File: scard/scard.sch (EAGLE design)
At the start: 49 parts, among them Q1 IRFD9210, X1 COAX

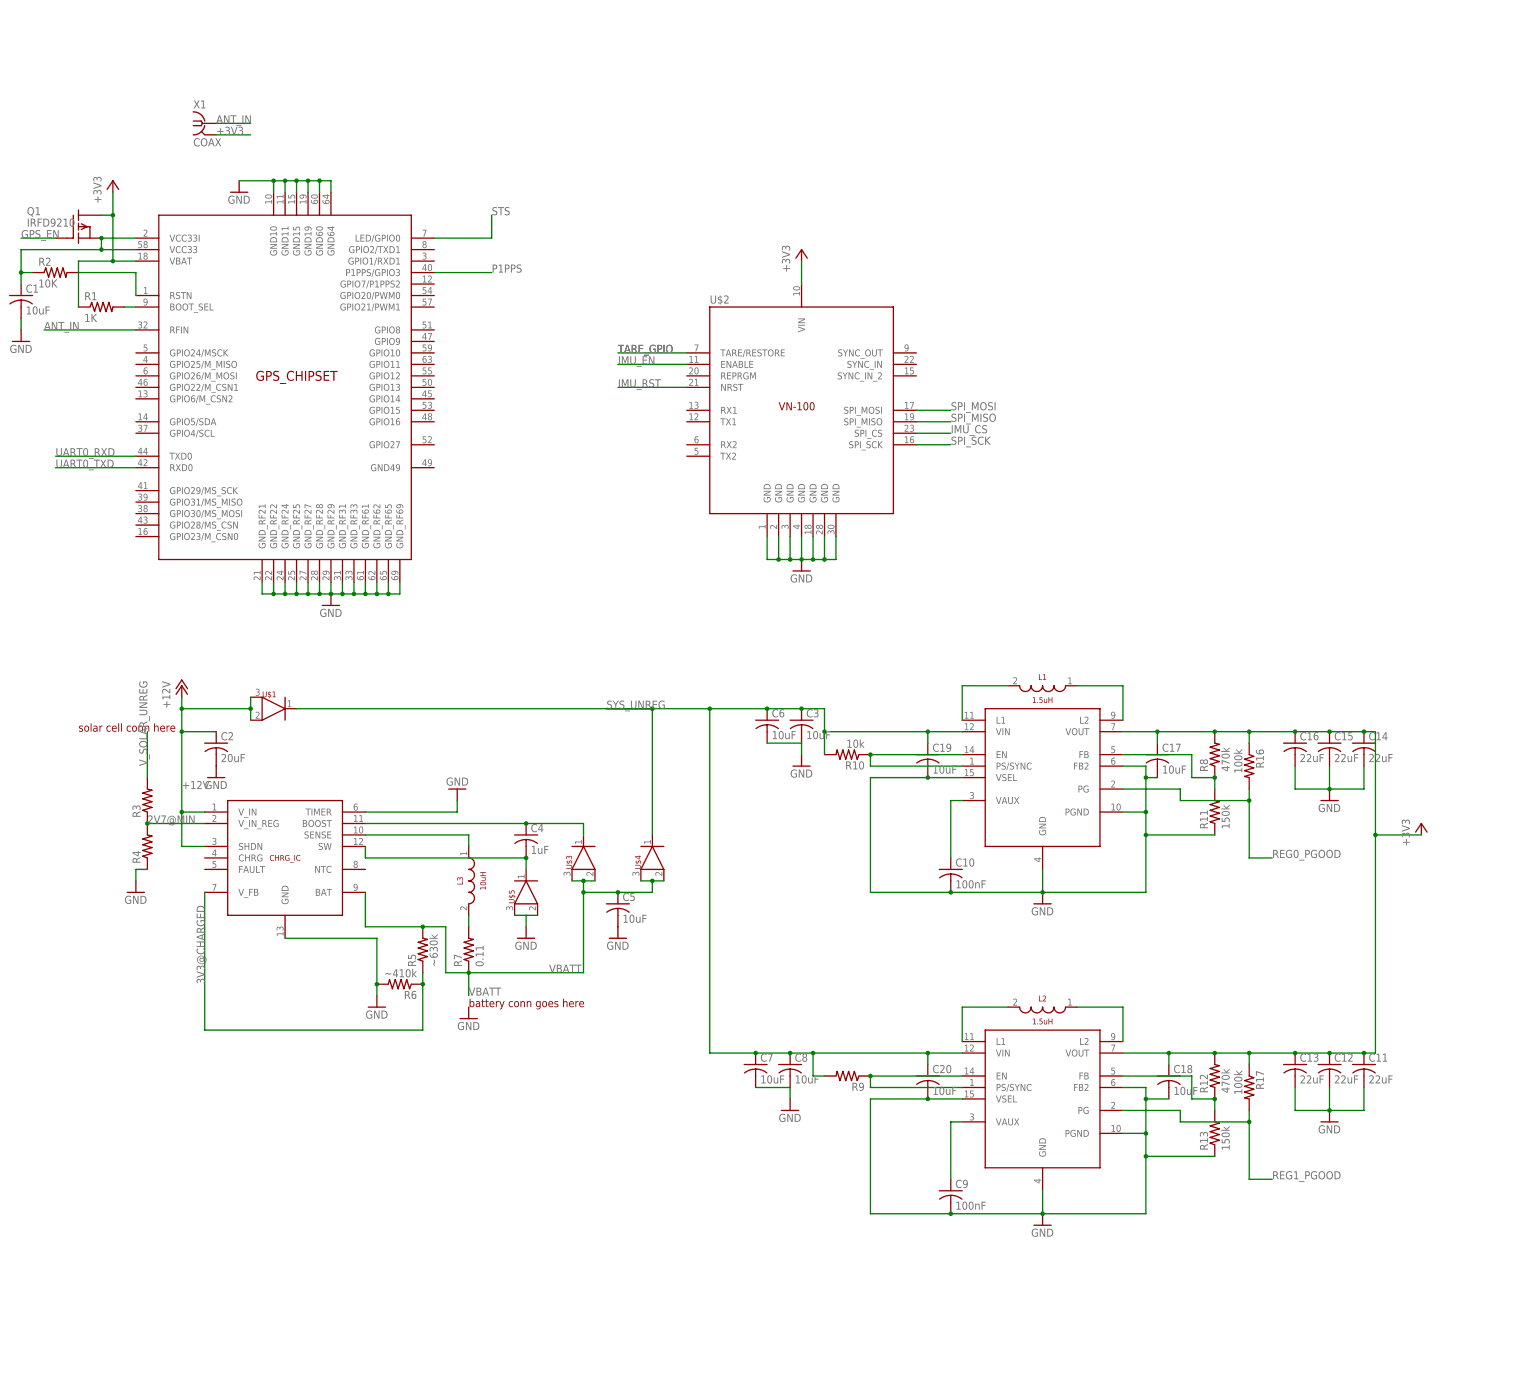
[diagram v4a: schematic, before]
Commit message: added voltage and current telemetry to battery and 3v3 regulators via an 8 channel adc
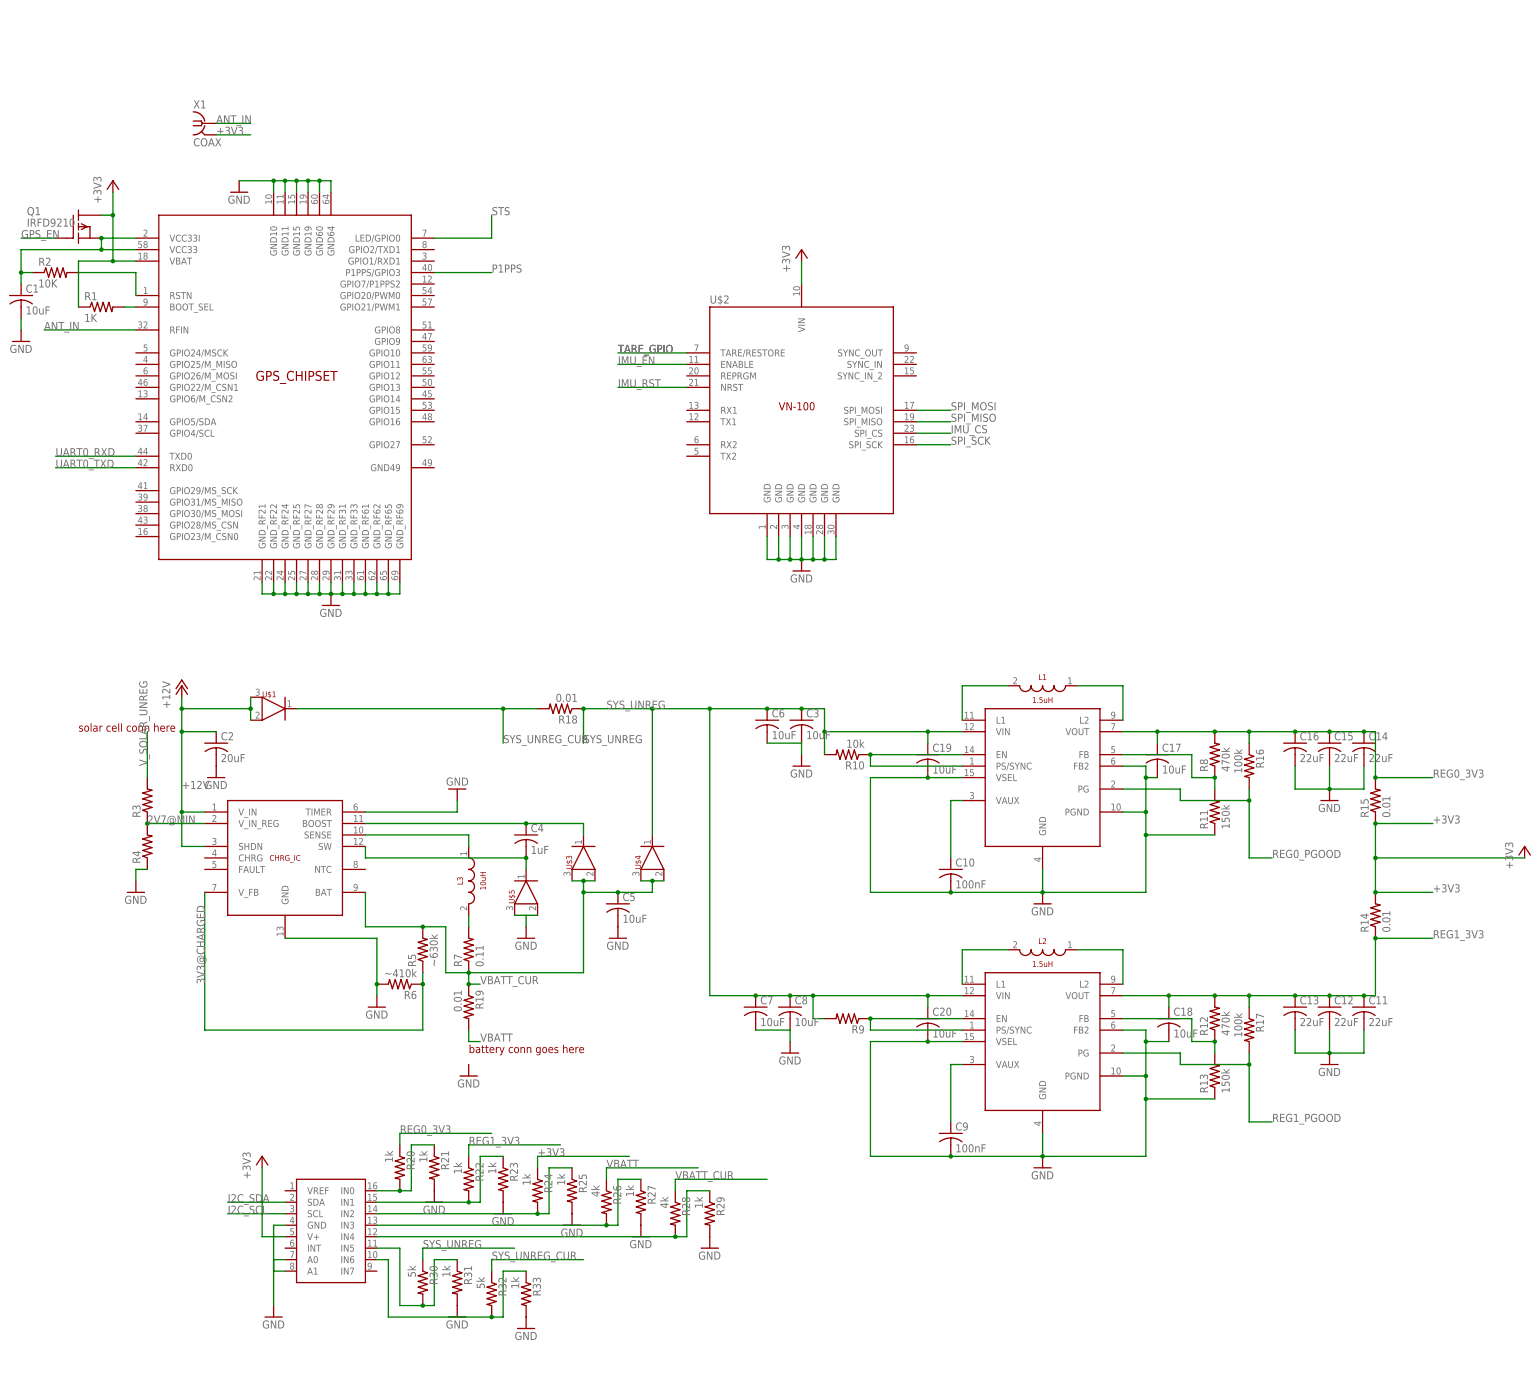
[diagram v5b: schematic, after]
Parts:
- added R14, R15, R18, R19: 0.01, resistor:R-US_R0603
- added R20, R21, R22, R23, R24, R25, R27, R29, R31, R33: 1k, resistor:R-US_R0603
- added R26, R28: 4k, resistor:R-US_R0603
- added R30, R32: 5k, resistor:R-US_R0603
- added U$9: ADC128D818, adc:ADC128D818
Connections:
- new net I2C_SCL: U$9.SCL
- new net I2C_SDA: U$9.SDA
- new net N$16: R20.2, R21.1, U$9.IN0
- new net N$17: R22.2, R23.1, U$9.IN1
- new net N$18: R24.2, R25.1, U$9.IN2
- new net N$19: R26.2, R27.1
- new net N$20: R28.2, R29.1
- new net N$21: R30.2, R31.1, U$9.IN5
- new net N$23: R32.2, R33.1, U$9.IN6
- new net REG0_3V3: C14.1, C15.1, C16.1, C17.1, R15.2, R16.1, R20.1, R8.2, U$6.VOUT
- new net REG1_3V3: C11.1, C12.1, C13.1, C18.1, R12.2, R14.1, R17.1, R22.1, U$7.VOUT
- new net SYS_UNREG_CUR: R18.2, R32.1, U$1.@3
- new net VBATT_CUR: C5.1, CHRG_IC.BAT, R19.1, R28.1, R5.2, R7.1, U$3.@1, U$3.@2, U$4.@1, U$4.@2
- net +3V3: now also R14.2, R15.1, R24.1, U$9.V+; no longer C11.1, C12.1, C13.1, C14.1, C15.1, C16.1, C17.1, C18.1, R12.2, R16.1, R17.1, R8.2, U$6.VOUT, U$7.VOUT
- net GND: now also R21.2, R23.2, R25.2, R27.2, R29.2, R31.2, R33.2, U$9.A0, U$9.A1, U$9.GND
- net SYS_UNREG: now also R18.1, R30.1; no longer U$1.@3
- net VBATT: now also R19.2, R26.1; no longer C5.1, CHRG_IC.BAT, R5.2, R7.1, U$3.@1, U$3.@2, U$4.@1, U$4.@2
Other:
- moved on the sheet: C11, C12, C13, C18, C20, C7, C8, C9, L2, R12, R13, R17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

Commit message: first stage of layout for power systems
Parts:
- added C21: 10uF, resistor:C-USC0603
- Q1: value IRFD9210 -> FDN360P; device transistor-fet:IRFD9210 -> transistor-power:FDN360P
- R14, R15, R18, R19: device resistor:R-US_R0603 -> resistor:R-US_R1210
- R9: value (none) -> 10k
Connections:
- net +3V3: now also C21.1
- net GND: now also C21.2

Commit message: finished test board v0.1 layout and added pictures
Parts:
- added C22: 10uF, resistor:C-USC0603
- added L4: 33nH, calsat:XFL4020
- added X2: 1365-20, con-leotronics:1365-20
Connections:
- net +12V: now also X2-18.S
- net +3V3: now also C22.1, L4.@1, X2-19.S; no longer X1COAX.GND
- net ANT_IN: now also L4.@2
- net GND: now also C22.2, C3.2, X1COAX.GND, X2-17.S, X2-20.S
- net GPS_EN: now also X2-10.S
- net I2C_SCL: now also X2-3.S
- net I2C_SDA: now also X2-1.S
- net IMU_CS: now also X2-6.S
- net IMU_EN: now also X2-8.S
- net IMU_RST: now also X2-13.S
- net N$19: now also U$9.IN3
- net N$20: now also U$9.IN4
- net P1PPS: now also X2-12.S
- net SPI_MISO: now also X2-7.S
- net SPI_MOSI: now also X2-9.S
- net SPI_SCK: now also X2-5.S
- net STS: now also X2-15.S
- net TARE_GPIO: now also X2-11.S
- net UART0_RXD: now also X2-2.S
- net UART0_TXD: now also X2-4.S
- net VBATT: now also X2-14.S, X2-16.S

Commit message: changes from design review
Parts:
- removed R20, R21, R22, R23, R24, R25, R27, R29, R31, R33: 1k, resistor:R-US_R0603
- removed R26, R28: 4k, resistor:R-US_R0603
- removed R30, R32: 5k, resistor:R-US_R0603
- removed U$3: B085BM30, calsat:B085BM30
- removed U$9: ADC128D818, adc:ADC128D818
- added A1, A3: INA3221-Q1, calsat:INA3221-Q1
- added C23, C24: 0.1uF, resistor:C-USC0603
- added D1: ES2D, diode:ES2D
- added PAD1, PAD2, PAD3, PAD4, PAD5: (no value), wirepad:SMD5
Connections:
- removed net N$16: R20.2, R21.1, U$9.IN0
- removed net N$17: R22.2, R23.1, U$9.IN1
- removed net N$18: R24.2, R25.1, U$9.IN2
- removed net N$19: R26.2, R27.1, U$9.IN3
- removed net N$2: CHRG_IC.SENSE, L3.@1
- removed net N$20: R28.2, R29.1, U$9.IN4
- removed net N$21: R30.2, R31.1, U$9.IN5
- removed net N$23: R32.2, R33.1, U$9.IN6
- new net N$32: A3.IN+2
- new net N$33: A3.IN-2
- new net N$34: A3.IN+3
- new net N$35: A3.IN-3
- net +12V: now also PAD4.P, PAD5.P; no longer X2-18.S
- net +3V3: now also A1.IN-1, A1.IN-2, A1.VS, A3.VS, C23.1, C24.1, PAD3.P; no longer R24.1, U$9.V+, X2-19.S
- net GND: now also A1.GND, A1.GND@2, A3.A0, A3.GND, A3.GND@2, C23.2, C24.2, PAD1.P, PAD2.P, X2-19.S; no longer R21.2, R23.2, R25.2, R27.2, R29.2, R31.2, R33.2, U$9.A0, U$9.A1, U$9.GND
- net I2C_SCL: now also A1.SCL, A3.SCL; no longer U$9.SCL
- net I2C_SDA: now also A1.A0, A1.SDA, A3.SDA; no longer U$9.SDA
- net N$3: now also D1.C; no longer U$3.@3
- net N$4: now also L3.@1
- net N$6: now also CHRG_IC.SENSE
- net REG0_3V3: now also A1.IN+1; no longer R20.1
- net REG1_3V3: now also A1.IN+2; no longer R22.1
- net SYS_UNREG: now also A3.IN-1; no longer R30.1
- net SYS_UNREG_CUR: now also A3.IN+1; no longer R32.1
- net VBATT: now also A1.IN-3, X2-18.S; no longer R26.1
- net VBATT_CUR: now also A1.IN+3, D1.A; no longer R28.1, U$3.@1, U$3.@2
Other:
- moved on the sheet: L3
